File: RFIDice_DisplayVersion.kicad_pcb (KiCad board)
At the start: 2 copper layers, 50.8 x 50.8 mm, 73 parts, among them J1 Conn_01x02, J2 CORTEX_JTAG_DEBUG_MINIMUM_PTH, Q1 Q_NMOS_DGS, SW1 SW_Push, SW2 SW_Push, SW3 SW_Push, SW4 SW_Push, SW5 SW_Push, SW6 , U1 LM4040DBZ-3, U2 MCP73831T-2ACI/OT, U3 MIC5219-3.3YM5, U4 RP2040, U5 Display, U6 W25Q128JVS, U7 PN532, X1 USB_C, Y1 ABLS-12.000MHZ-B4-T

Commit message: Gonna go back and change start from power instead
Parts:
- added U$6: , AndyKiCadLibrary:MOUNTINGHOLE_3.0, F.Cu at (82.0, 77.0)
- added U$6: , AndyKiCadLibrary:MOUNTINGHOLE_3.0, F.Cu at (43.0, 77.0)
- moved U7 303.9 mm to (53.3, 74.4), turned to 90 degrees
- moved R14 292.6 mm to (66.5, 78.0)
- moved R15 292.6 mm to (66.5, 80.5)
- moved U5 270.7 mm to (90.2, 90.2)
- moved TP1 204.7 mm to (115.6, 74.3)
- moved TP10 204.7 mm to (115.6, 67.4)
- moved TP13 204.7 mm to (128.6, 67.4)
- moved TP14 204.7 mm to (101.4, 92.8)
- moved TP2 204.7 mm to (115.6, 81.1)
- moved TP4 204.7 mm to (124.3, 67.4)
- moved TP5 204.7 mm to (101.4, 97.2)
- moved TP7 204.7 mm to (124.3, 76.8)
- moved TP8 204.7 mm to (120.0, 81.8)
- moved TP9 204.7 mm to (111.3, 80.5)
- moved TP11 204.7 mm to (97.1, 90.6)
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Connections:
- C1 pad 2: GND1 -> -BATT
- D1 pad 2: Net-(D1-Pad2) -> +5V
- R2 pad 2: GND1 -> -BATT
- R3 pad 1: +5V -> Net-(D1-Pad1)
- R3 pad 2: Net-(D1-Pad2) -> Net-(R3-Pad2)
- U2 pad 1: Net-(D1-Pad1) -> Net-(R3-Pad2)
- U2 pad 2: GND1 -> -BATT
- X1 pad M1: -BATT -> (no net)
- X1 pad M2: -BATT -> (no net)
- X1 pad M3: -BATT -> (no net)
- X1 pad M4: -BATT -> (no net)
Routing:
- net +3V3: track 19.8 -> 43.9 mm
- net -BATT: track 23.6 -> 44.2 mm
- net +BATT: track 0.00 -> 17.4 mm
- net +5V: track 7.89 -> 22.5 mm
- net GND: track 1.65 -> 14.5 mm, vias 1 -> 7
- net /QSPI_SS: track 13.5 -> 7.80 mm
- net /QSPL_SD1: track 12.5 -> 7.05 mm
- net /QSPL_SD2: track 10.9 -> 6.18 mm
- net Net-(R2-Pad1): track 0.00 -> 2.30 mm
- net Net-(R3-Pad2): track 0.00 -> 2.09 mm
- net Net-(D1-Pad1): track 0.00 -> 1.96 mm
- net /QSPI_SCLK: track 16.8 -> 14.9 mm
- net /QSPL_SD3: track 18.9 -> 17.3 mm
- net /UART0_TX: track 4.08 -> 5.66 mm
- net /UART0_RX: track 4.35 -> 5.66 mm
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- added copper zone on F.Cu, net +5V
- added copper zone on F.Cu, net +BATT
- added copper zone on F.Cu, net -BATT

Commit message: Maybe probably finished
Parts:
- removed TP14, TP15, TP18, TP3: TestPoint, TestPoint:TestPoint_Keystone_5000-5004_Miniature
- added U$6: , AndyKiCadLibrary:MOUNTINGHOLE_3.0, F.Cu at (73.5, 112.5)
- moved X1 81.7 mm to (116.0, 79.1), turned to 90 degrees
- moved J1 75.2 mm to (109.6, 71.5), turned to 90 degrees
- moved R4 72.4 mm to (112.4, 85.5), turned to 180 degrees
- moved R5 72.1 mm to (112.4, 87.2), turned to 180 degrees
- moved BATT1 71.1 mm to (111.0, 95.0), turned to 180 degrees
- moved R13 65.2 mm to (105.0, 73.5), turned to 180 degrees
- moved R12 63.8 mm to (105.0, 75.1), turned to 180 degrees
- moved TP4 60.5 mm to (68.3, 90.4), turned to 180 degrees
- moved C20 59.8 mm to (96.0, 66.9)
- moved Q1 58.4 mm to (104.9, 100.8), turned to 180 degrees
- moved TP10 55.8 mm to (68.6, 97.4), turned to 180 degrees
- moved R9 55.6 mm to (106.9, 104.4)
- moved C6 54.1 mm to (102.5, 96.1), turned to 180 degrees
- moved C1 53.3 mm to (102.5, 83.7), turned to 180 degrees
- moved SW6 53.0 mm to (100.7, 105.0)
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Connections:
- U4 pad 11: /BTN3 -> unconnected-(U4-Pad11)
- U4 pad 12: /BTN4 -> unconnected-(U4-Pad12)
- U4 pad 13: /BTN5 -> unconnected-(U4-Pad13)
- U4 pad 34: unconnected-(U4-Pad34) -> /BTN1
- U4 pad 35: unconnected-(U4-Pad35) -> /BTN2
- U4 pad 36: unconnected-(U4-Pad36) -> /BTN3
- U4 pad 37: unconnected-(U4-Pad37) -> /BTN4
- U4 pad 39: unconnected-(U4-Pad39) -> /BTN5
- U4 pad 8: /BTN1 -> unconnected-(U4-Pad8)
- U4 pad 9: /BTN2 -> unconnected-(U4-Pad9)
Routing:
- net +3V3: track 43.9 -> 267.1 mm, vias 0 -> 2
- net +BATT: track 17.4 -> 116.8 mm, vias 0 -> 3
- net GND: track 14.5 -> 75.5 mm, vias 7 -> 19
- net /BTN3: track 4.28 -> 50.1 mm, vias 0 -> 4
- net /BTN2: track 4.93 -> 50.4 mm, vias 0 -> 6
- net /BTN4: track 4.09 -> 48.5 mm, vias 0 -> 4
- net /SPI_CS: track 0.00 -> 36.1 mm, vias 0 -> 2
- net /BTN1: track 5.34 -> 41.2 mm, vias 0 -> 4
- net /SPI_TX: track 0.00 -> 35.5 mm, vias 0 -> 2
- net -BATT: track 44.2 -> 75.4 mm, vias 0 -> 1
- net /SPI_RX: track 1.43 -> 30.8 mm
- net /SPI_SCK: track 0.00 -> 28.6 mm
- net /BTN5: track 3.87 -> 32.2 mm, vias 0 -> 4
- net /DISP_DATA/COMMAND: track 0.00 -> 27.7 mm
- net /I2C0_SDA: track 4.35 -> 31.7 mm
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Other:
- board size 50.8 x 50.8 mm -> 50.8 x 78.3 mm

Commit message: Commented on PCB
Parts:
- renumbered TP4 to +3.3V, TP2 to +BATT, TP1 to -BATT, TP9 to CS, TP8 to D/C, TP5 to GND, TP16 to I2C_CK, TP17 to I2C_SDA, TP13 to RFID_IRQ, TP6 to RX, TP12 to RX, TP11 to SPI_SCK, TP10 to TX, TP7 to UART_TX
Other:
- board text added: "+"
- board text added: "+3.3V"
- board text added: "+BATT"
- board text added: "D/C"
- board text added: "GND"
- board text added: "RST"
- board text added: "SCK"
- board text added: "SPI_CS"
- board text added: "SPI_RX"
- board text added: "SPI_TX"

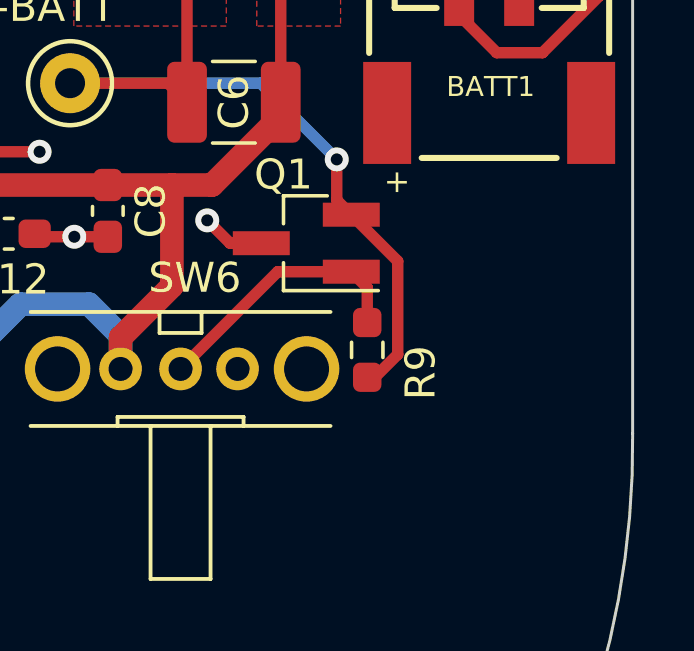
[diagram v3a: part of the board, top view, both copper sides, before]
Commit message: Fixed cutout section
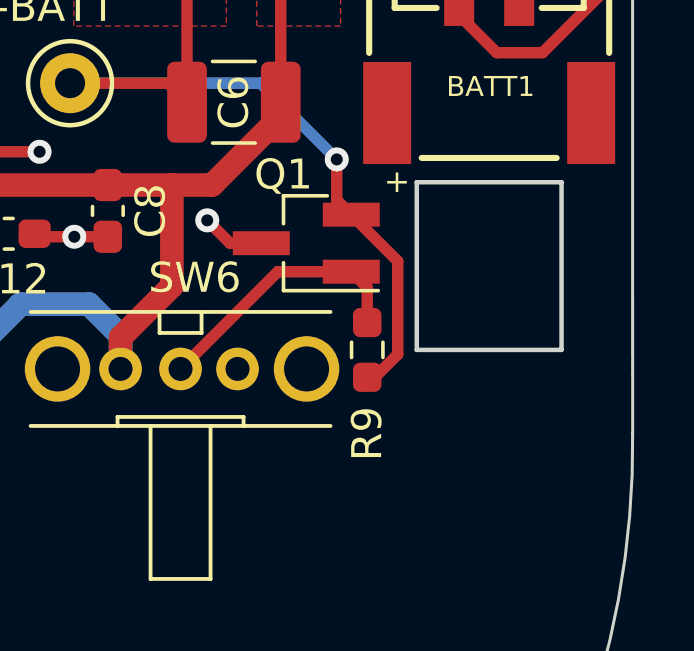
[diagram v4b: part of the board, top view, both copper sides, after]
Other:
- outline, holes or cut-outs redrawn
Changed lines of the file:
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@@
     (property "Sheetname" "")
     (attr smd)
-    (fp_text reference "R9" (at 0.762 -1.778 90) (layer "F.SilkS")
+    (fp_text reference "R9" (at 2.794 0 90) (layer "F.SilkS")
       (effects (font (size 1 1) (thickness 0.15)))
     )
@@
     )
   )
-  (gr_rect (start 108.585 98.298) (end 113.411 103.886) (layer "Dwgs.User") (width 0.15) (fill none))
   (gr_line (start 115.774 56.381) (end 115.781 107.181) (layer "Edge.Cuts") (width 0.1))
   (gr_arc (start 84.638091 134.627) (mid 70.307125 124.132999) (end 64.981 107.188) (layer "Edge.Cuts") (width 0.1))
@@
   (gr_line (start 64.974 56.388) (end 115.774 56.381) (layer "Edge.Cuts") (width 0.1))
   (gr_line (start 64.981 107.188) (end 64.974 56.388) (layer "Edge.Cuts") (width 0.1))
+  (gr_rect (start 108.585 98.806) (end 113.411 104.394) (layer "Edge.Cuts") (width 0.15) (fill none))
   (gr_text "SPI_CS\n" (at 78.232 107.188 270) (layer "F.SilkS")
     (effects (font (size 0.762 0.762) (thickness 0.1905)))
@@
       )
     )
-  )
-  (zone (net 0) (net_name "") (layer "Edge.Cuts") (hatch edge 0.508)
-    (connect_pads yes (clearance 0))
-    (min_thickness 0.254)
-    (keepout (tracks not_allowed) (vias not_allowed) (pads not_allowed) (copperpour not_allowed) (footprints allowed))
-    (fill (thermal_gap 0.508) (thermal_bridge_width 0.508))
-    (polygon
-      (pts
-        (xy 108.585 98.298)
-        (xy 113.411 98.298)
-        (xy 113.411 103.886)
-        (xy 108.585 103.886)
-      )
-    )

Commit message: Probably final commit
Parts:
- added  : LOGO, LOGO, F.Cu at (110.7, 109.0)
- renumbered RX to UART_RX
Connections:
- X1 pad M1: (no net) -> -BATT
- X1 pad M2: (no net) -> -BATT
- X1 pad M3: (no net) -> -BATT
- X1 pad M4: (no net) -> -BATT
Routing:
- net /PN532_RSTOUT_N: track 18.2 -> 17.6 mm, vias 2 -> 1
- net /UART0_TX: track 10.1 -> 10.7 mm, vias 2 -> 1
- net /UART0_RX: track 12.5 -> 12.3 mm, vias 2 -> 1
- net /PN532_IRQ: vias 2 -> 1
- net /BTN2: vias 6 -> 4
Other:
- board text added: "RFIDice Tray By: Andy Troyer"
